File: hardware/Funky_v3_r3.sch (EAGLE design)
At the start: 43 parts, among them IC2 LTC3525, IC3 MCP1703CB, Q1 P-MOSFET, U3 ATMEGA32U4, Y1 8MHz

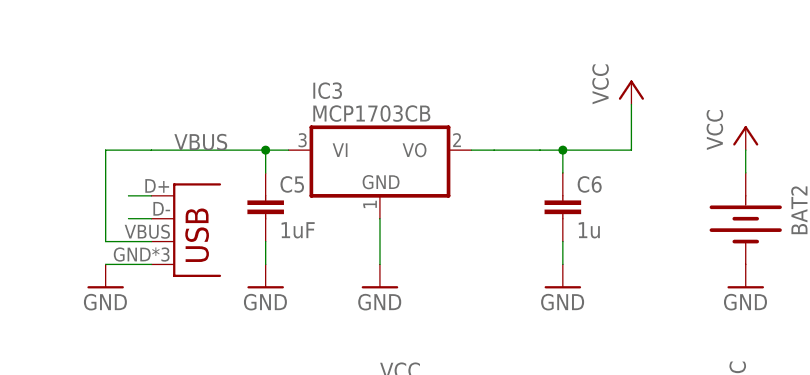
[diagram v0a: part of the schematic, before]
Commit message: Hardware update
Node 1.0.0, export and node shield
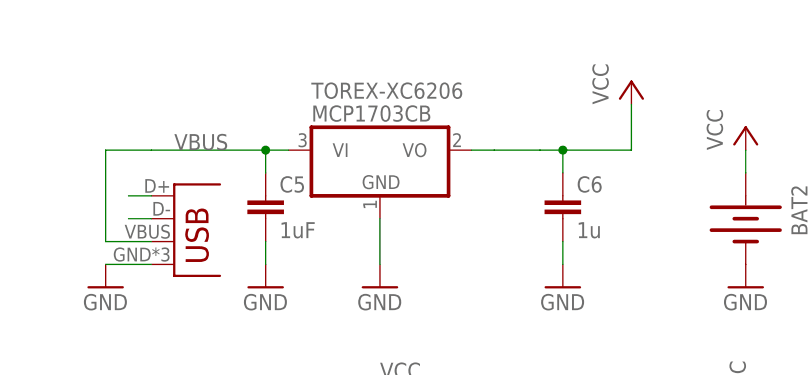
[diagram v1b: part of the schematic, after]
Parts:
- renumbered IC3 to TOREX-XC6206
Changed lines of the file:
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@@
 <?xml version="1.0" encoding="utf-8"?>
 <!DOCTYPE eagle SYSTEM "eagle.dtd">
-<eagle version="6.3">
+<eagle version="6.1">
 <drawing>
 <settings>
@@
 <part name="L1" library="SparkFun" deviceset="INDUCTOR" device="1210" value="10 µH"/>
 <part name="P+9" library="supply1" deviceset="VCC" device=""/>
-<part name="IC3" library="linear" deviceset="MCP1703" device="CB"/>
+<part name="TOREX-XC6206" library="linear" deviceset="MCP1703" device="CB"/>
 <part name="C5" library="rcl" deviceset="C-EU" device="C0603K" value="1uF"/>
 <part name="C6" library="rcl" deviceset="C-EU" device="C0603K" value="1u"/>
@@
 <instance part="L1" gate="G$1" x="33.02" y="124.46" rot="R90"/>
 <instance part="P+9" gate="VCC" x="68.58" y="124.46"/>
-<instance part="IC3" gate="G$1" x="116.84" y="121.92"/>
+<instance part="TOREX-XC6206" gate="G$1" x="116.84" y="121.92"/>
 <instance part="C5" gate="G$1" x="104.14" y="116.84"/>
 <instance part="C6" gate="G$1" x="137.16" y="116.84"/>
@@
 <wire x1="137.16" y1="119.38" x2="137.16" y2="121.92" width="0.1524" layer="91"/>
 <junction x="137.16" y="121.92"/>
-<pinref part="IC3" gate="G$1" pin="VO"/>
+<pinref part="TOREX-XC6206" gate="G$1" pin="VO"/>
 <wire x1="129.54" y1="121.92" x2="127" y2="121.92" width="0.1524" layer="91"/>
 <wire x1="134.62" y1="121.92" x2="129.54" y2="121.92" width="0.1524" layer="91"/>
@@
 </segment>
 <segment>
-<pinref part="IC3" gate="G$1" pin="GND"/>
+<pinref part="TOREX-XC6206" gate="G$1" pin="GND"/>
 <pinref part="GND9" gate="1" pin="GND"/>
 <wire x1="116.84" y1="109.22" x2="116.84" y2="114.3" width="0.1524" layer="91"/>
@@
 <net name="VBUS" class="1">
 <segment>
-<pinref part="IC3" gate="G$1" pin="VI"/>
+<pinref part="TOREX-XC6206" gate="G$1" pin="VI"/>
 <wire x1="106.68" y1="121.92" x2="104.14" y2="121.92" width="0.1524" layer="91"/>
 <pinref part="C5" gate="G$1" pin="1"/>
